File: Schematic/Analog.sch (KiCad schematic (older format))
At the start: 25 parts, among them J1 GS3, SW1 SW_Push_Dual, SW2 SW_Push_Dual, U1 QX14T50B3.6864

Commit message: Brought the schematic and PCB board design up to date.
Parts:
- removed C2: 10uF, Capacitors_THT:CP_Radial_D5.0mm_P2.50mm, symbol CP
- added C20, C21, C22: 0.1uF, Capacitors_THT:C_Disc_D4.7mm_W2.5mm_P5.00mm, symbol C_Small
- added D1: 1N4148, Diodes_THT:D_DO-35_SOD27_P2.54mm_Vertical_AnodeUp, symbol D
- added IC18: NE555, Housings_DIP:DIP-8_W7.62mm_Socket, symbol NE555
- added J2: DataBus Pin Header, Socket_Strips:Socket_Strip_Straight_1x10_Pitch2.54mm, symbol Conn_01x10_Male
- added J3: AddressBus Pin Header, Socket_Strips:Socket_Strip_Straight_1x18_Pitch2.54mm, symbol Conn_01x18_Male
- added R4: 1M, Resistors_THT:R_Axial_DIN0204_L3.6mm_D1.6mm_P1.90mm_Vertical, symbol R
- added R5, R6: 10K, Resistors_THT:R_Axial_DIN0204_L3.6mm_D1.6mm_P1.90mm_Vertical, symbol R
- C1: footprint Capacitors_THT:CP_Radial_D5.0mm_P2.50mm -> Capacitors_THT:CP_Radial_D5.0mm_P2.00mm
- C10, C11, C12, C13, C14, C15, C16, C17, C18, C19, C4, C5, C6, C7, C8, C9: footprint Capacitors_THT:C_Disc_D3.0mm_W1.6mm_P2.50mm -> Capacitors_THT:C_Disc_D4.7mm_W2.5mm_P5.00mm
- C3: footprint Capacitors_THT:CP_Radial_D10.0mm_P2.50mm -> Capacitors_THT:CP_Radial_D8.0mm_P5.00mm
- J1: footprint Connectors:GS3 -> Pin_Headers:Pin_Header_Straight_1x03_Pitch2.54mm
- R1: value 10K -> 20K
- R2: value 10K -> 1K
- U1: value QX14T50B3.6864 -> ECS-100A-035
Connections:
- net GNDREF: now also SW1.3, SW2.3, C20.2, C21.2, IC18.1 (GND), J2.1 (Pin_1), J3.1 (Pin_1); no longer SW1.4, SW2.4
- net VCC: now also C20.1, D1.1 (K), IC18.4 (R), IC18.8 (VCC), R4.1, R5.1, R6.1; no longer R2.1
- net Reset renamed ~Reset
- net ~Reset: now also R2.1; no longer SW1.3
- new net: R2.2, SW1.4
- new net: IC18.3 (Q), J1.3 (G3)
- new net: C22.2, R6.2, SW2.4
- new net: C22.1, D1.2 (A), IC18.2 (TR), R5.2
- new net: C21.1, IC18.6 (THR), IC18.7 (DIS), R4.2
- new net adr0: J3.3 (Pin_3)
- new net adr1: J3.4 (Pin_4)
- new net adr10: J3.13 (Pin_13)
- new net adr11: J3.14 (Pin_14)
- new net adr12: J3.15 (Pin_15)
- new net adr13: J3.16 (Pin_16)
- new net adr14: J3.17 (Pin_17)
- new net adr15: J3.18 (Pin_18)
- new net adr2: J3.5 (Pin_5)
- new net adr3: J3.6 (Pin_6)
- new net adr4: J3.7 (Pin_7)
- new net adr5: J3.8 (Pin_8)
- new net adr6: J3.9 (Pin_9)
- new net adr7: J3.10 (Pin_10)
- new net adr8: J3.11 (Pin_11)
- new net adr9: J3.12 (Pin_12)
- new net d0: J2.3 (Pin_3)
- new net d1: J2.4 (Pin_4)
- new net d2: J2.5 (Pin_5)
- new net d3: J2.6 (Pin_6)
- new net d4: J2.7 (Pin_7)
- new net d5: J2.8 (Pin_8)
- new net d6: J2.9 (Pin_9)
- new net d7: J2.10 (Pin_10)
- no-connect marks 5 -> 8
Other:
- note added: "3.5MHz oscillator"
- note added: "555 circuit from https://electronics.stackexchange.com/questions/180716/555-timer-one-shot-trigger"
- note added: "AddressBus"
- note added: "Clock generation"
- note added: "DataBus"
- note added: "Logic levels"
- note added: "Reset generation"
- note removed: "3.68MHz oscillator"
- moved on the sheet: C1, C10, C11, C12, C13, C14, C15, C16, C17, C18, C19, C3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

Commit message: Brought the schematic up to date with the wiring from the TTL verilog version.
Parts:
- added IC15: 74HCT139, symbol 74LS139
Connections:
- net Clk: now also IC15.14 (A0)
- net GNDREF: now also IC15.13 (A1), IC15.15 (E)
- net VCC: now also IC15.16 (VCC)
- new net GND: IC15.8 (GND)
- no-connect marks 8 -> 11
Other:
- note added: "Clkbar is an inverted Clk signal, used to initiate events on the\nfalling edge of Clk. We use the spare 139 half as an inverter."
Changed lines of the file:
@@
 Text Notes 750  7650 0    60   ~ 0
 555 circuit from https://electronics.stackexchange.com/questions/180716/555-timer-one-shot-trigger
+$Comp
+L 74LS139 IC15
+U 2 1 5CC0FB47
+P 7750 4700
+F 0 "IC15" H 7750 5250 50  0000 C CNN
+F 1 "74HCT139" H 7750 5150 50  0000 C CNN
+F 2 "" H 7750 4700 50  0001 C CNN
+F 3 "" H 7750 4700 50  0001 C CNN
+	2    7750 4700
+	1    0    0    -1
+$EndComp
+Text GLabel 6650 4600 0    60   Input ~ 0
+Clk
+Wire Wire Line
+	6900 4600 6650 4600
+Text GLabel 6600 4450 0    60   Input ~ 0
+Lo
+Text GLabel 6600 4950 0    60   Input ~ 0
+Lo
+Wire Wire Line
+	6600 4450 6900 4450
+Wire Wire Line
+	6600 4950 6900 4950
+Text GLabel 9250 4600 0    60   Output ~ 0
+~Clkbar
+Wire Wire Line
+	8600 4600 8900 4600
+NoConn ~ 8600 4400
+NoConn ~ 8600 4800
+NoConn ~ 8600 5000
+Text Notes 6400 5400 0    60   ~ 0
+Clkbar is an inverted Clk signal, used to initiate events on the\nfalling edge of Clk. We use the spare 139 half as an inverter.
 $EndSCHEMATC

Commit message: Updated the schematic and also moved to KiCad 5.
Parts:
- removed J1: GS3, Pin_Headers:Pin_Header_Straight_1x03_Pitch2.54mm, symbol GS3
- removed J2: DataBus Pin Header, Socket_Strips:Socket_Strip_Straight_1x10_Pitch2.54mm, symbol Conn_01x10_Male
- removed J3: AddressBus Pin Header, Socket_Strips:Socket_Strip_Straight_1x18_Pitch2.54mm, symbol Conn_01x18_Male
- added J1: Jumper_3_Bridged12, Connector_PinSocket_2.54mm:PinSocket_1x03_P2.54mm_Vertical, symbol Jumper:Jumper_3_Bridged12
- added J2: Data Bus Pin Header, Connector_PinSocket_2.54mm:PinSocket_1x10_P2.54mm_Vertical, symbol Connector:Conn_01x10_Female
- added J3: Address Bus Pin Header, Connector_PinSocket_2.54mm:PinSocket_1x18_P2.54mm_Vertical, symbol Connector:Conn_01x18_Female
- C1, C3: symbol CP -> Device:CP
- C10, C11, C12, C13, C14, C15, C16, C17, C18, C19, C4, C5, C6, C7, C8, C9: symbol C -> Device:C
- C20, C21, C22: symbol C_Small -> Device:C_Small
- D1: symbol D -> Device:D
- IC15: footprint (none) -> Package_DIP:DIP-16_W7.62mm_Socket; symbol 74LS139 -> 74xx:74LS139
- IC18: symbol NE555 -> Timer:NE555
- R1, R2, R4, R5, R6: symbol R -> Device:R
- SW1, SW2: symbol SW_Push_Dual -> Switch:SW_Push_Dual
- U1: symbol QX14T50B1.843200B50TT -> QX14T50B1.843200B50TT:QX14T50B1.843200B50TT
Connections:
- net Clk: now also J1.2 (C)
- net GNDREF: now also J2.10 (Pin_10), J3.18 (Pin_18)
- net VCC: no longer IC15.16 (VCC)
- net adr0: now also J3.16 (Pin_16)
- net adr1: now also J3.15 (Pin_15)
- net adr10: now also J3.6 (Pin_6)
- net adr11: now also J3.5 (Pin_5)
- net adr12: now also J3.4 (Pin_4)
- net adr13: now also J3.3 (Pin_3)
- net adr14: now also J3.2 (Pin_2)
- net adr15: now also J3.1 (Pin_1)
- net adr2: now also J3.14 (Pin_14)
- net adr3: now also J3.13 (Pin_13)
- net adr4: now also J3.12 (Pin_12)
- net adr5: now also J3.11 (Pin_11)
- net adr6: now also J3.10 (Pin_10)
- net adr7: now also J3.9 (Pin_9)
- net adr8: now also J3.8 (Pin_8)
- net adr9: now also J3.7 (Pin_7)
- net d0: now also J2.8 (Pin_8)
- net d1: now also J2.7 (Pin_7)
- net d2: now also J2.6 (Pin_6)
- net d3: now also J2.5 (Pin_5)
- net d4: now also J2.4 (Pin_4)
- net d5: now also J2.3 (Pin_3)
- net d6: now also J2.2 (Pin_2)
- net d7: now also J2.1 (Pin_1)
- net ~Clkbar: now also IC15.11 (O1)
- net at U1.8 (OUTPUT): now also J1.3 (B)
- net at IC18.3 (Q): now also J1.1 (A)
- removed net GND: IC15.8 (GND)
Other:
- note added: "555 circuit from\nhttps://electronics.stackexchange.com/questions/180716/555-timer-one-shot-trigger"
- note removed: "555 circuit from https://electronics.stackexchange.com/questions/180716/555-timer-one-shot-trigger"

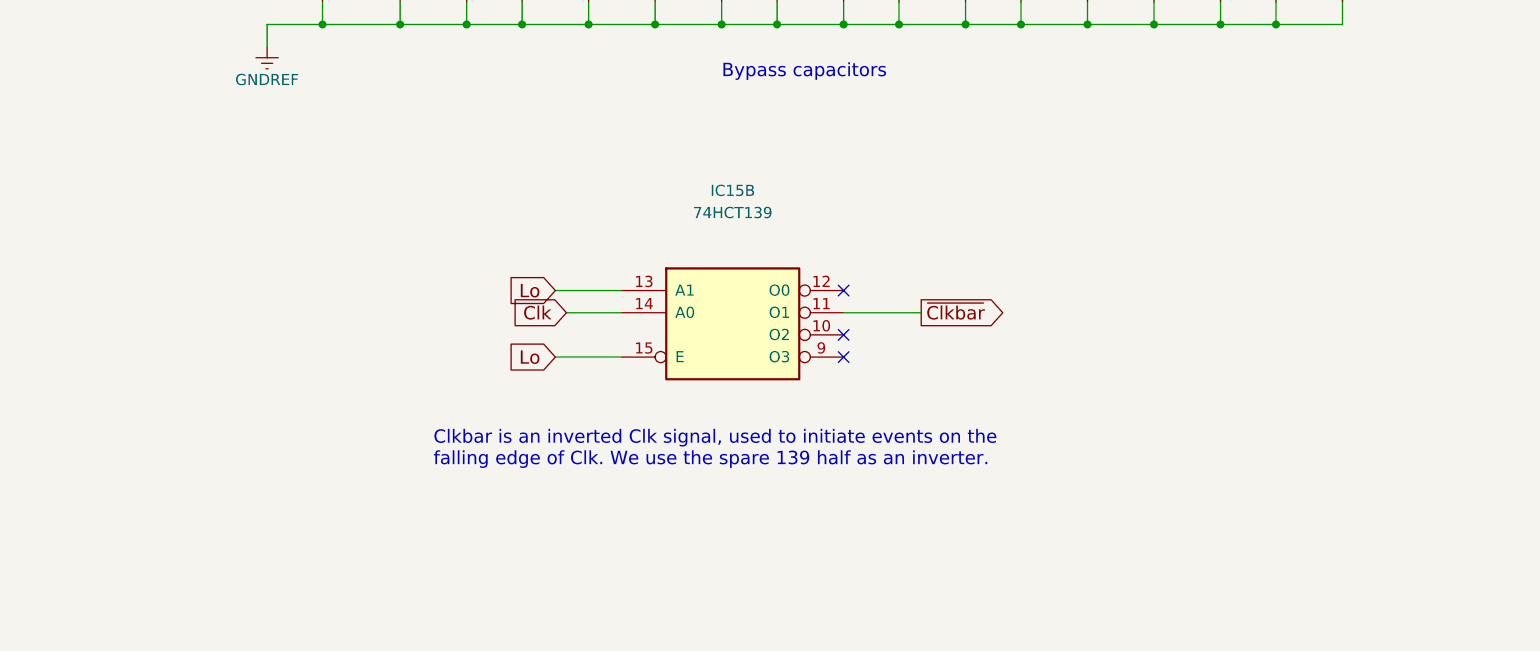
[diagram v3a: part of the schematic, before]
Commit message: Updated the PCB and schematic to have a 330pF capacitor to fix the "jump" glitch that I've been experiencing.
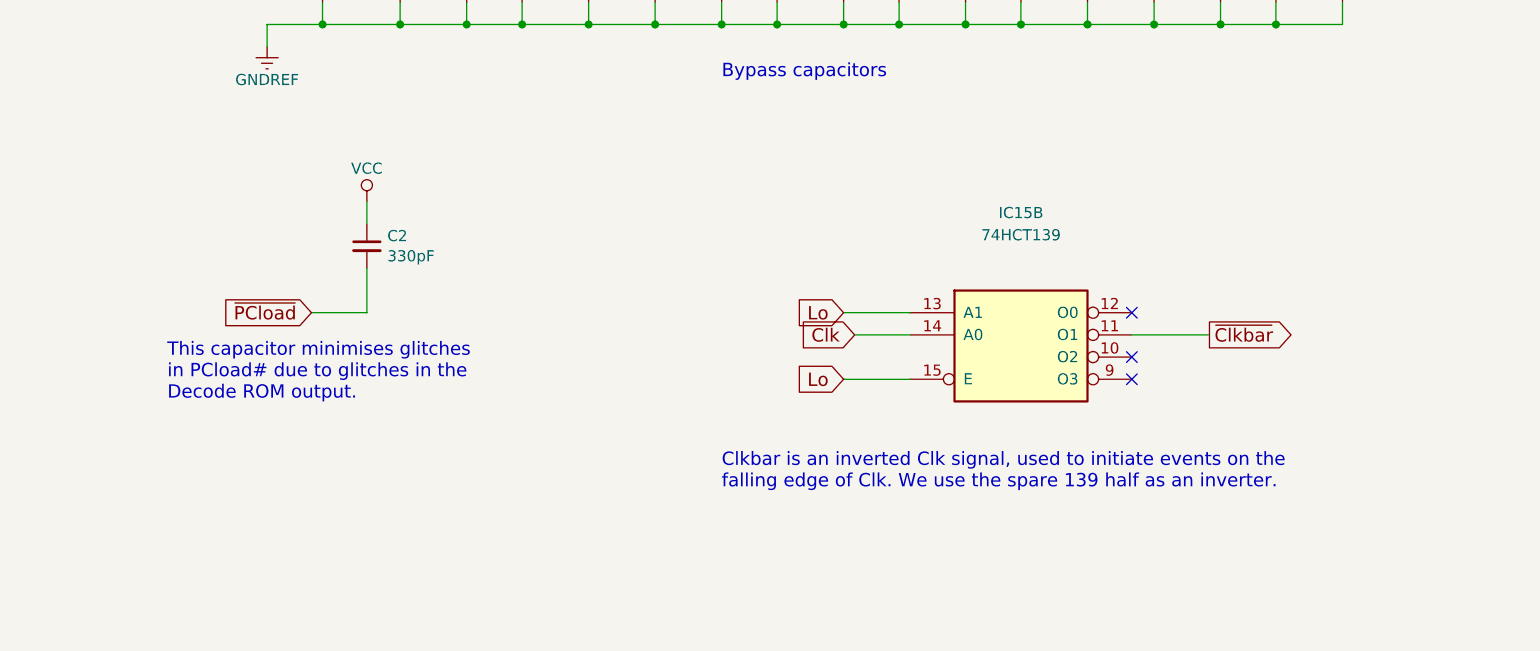
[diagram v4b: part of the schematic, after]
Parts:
- added C2: 330pF, Capacitor_THT:C_Disc_D4.7mm_W2.5mm_P5.00mm, symbol Device:C_Small
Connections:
- net VCC: now also C2.1
- new net ~PCload: C2.2
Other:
- note added: "This capacitor minimises glitches\nin PCload# due to glitches in the\nDecode ROM output."
- moved on the sheet: IC15B
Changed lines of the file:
@@
 L 74xx:74LS139 IC15
 U 2 1 5CC0FB47
-P 7750 4700
-F 0 "IC15" H 7750 5250 50  0000 C CNN
-F 1 "74HCT139" H 7750 5150 50  0000 C CNN
-F 2 "Package_DIP:DIP-16_W7.62mm_Socket" H 7750 4700 50  0001 C CNN
-F 3 "" H 7750 4700 50  0001 C CNN
-	2    7750 4700
+P 9050 4800
+F 0 "IC15" H 9050 5350 50  0000 C CNN
+F 1 "74HCT139" H 9050 5250 50  0000 C CNN
+F 2 "Package_DIP:DIP-16_W7.62mm_Socket" H 9050 4800 50  0001 C CNN
+F 3 "" H 9050 4800 50  0001 C CNN
+	2    9050 4800
 	1    0    0    -1
 $EndComp
-Text GLabel 7000 4700 0    60   Input ~ 0
+Text GLabel 8300 4800 0    60   Input ~ 0
 Clk
 Wire Wire Line
-	7250 4700 7000 4700
-Text GLabel 6950 4600 0    60   Input ~ 0
+	8550 4800 8300 4800
+Text GLabel 8250 4700 0    60   Input ~ 0
 Lo
-Text GLabel 6950 4900 0    60   Input ~ 0
+Text GLabel 8250 5000 0    60   Input ~ 0
 Lo
 Wire Wire Line
-	6950 4600 7250 4600
+	8250 4700 8550 4700
 Wire Wire Line
-	6950 4900 7250 4900
-Text GLabel 8600 4700 2    60   Output ~ 0
+	8250 5000 8550 5000
+Text GLabel 9900 4800 2    60   Output ~ 0
 ~Clkbar
-NoConn ~ 8250 4600
-NoConn ~ 8250 4800
-NoConn ~ 8250 4900
-Text Notes 6400 5400 0    60   ~ 0
+NoConn ~ 9550 4700
+NoConn ~ 9550 4900
+NoConn ~ 9550 5000
+Text Notes 7700 5500 0    60   ~ 0
 Clkbar is an inverted Clk signal, used to initiate events on the\nfalling edge of Clk. We use the spare 139 half as an inverter.
 Wire Wire Line
@@
 $EndComp
 Wire Wire Line
-	8250 4700 8600 4700
+	9550 4800 9900 4800
+Text GLabel 5850 4700 0    60   Input ~ 0
+~PCload
+$Comp
+L power:VCC #PWR0104
+U 1 1 5CF39113
+P 6100 4200
+F 0 "#PWR0104" H 6100 4050 50  0001 C CNN
+F 1 "VCC" H 6100 4350 50  0000 C CNN
+F 2 "" H 6100 4200 50  0001 C CNN
+F 3 "" H 6100 4200 50  0001 C CNN
+	1    6100 4200
+	1    0    0    -1
+$EndComp
+Wire Wire Line
+	6100 4200 6100 4300
+Text Notes 5200 5100 0    60   ~ 0
+This capacitor minimises glitches\nin PCload# due to glitches in the\nDecode ROM output.
+$Comp
+L Device:C_Small C2
+U 1 1 5CF599C2
+P 6100 4400
+F 0 "C2" H 6192 4446 50  0000 L CNN
+F 1 "330pF" H 6192 4355 50  0000 L CNN
+F 2 "Capacitor_THT:C_Disc_D4.7mm_W2.5mm_P5.00mm" H 6100 4400 50  0001 C CNN
+F 3 "~" H 6100 4400 50  0001 C CNN
+	1    6100 4400
+	1    0    0    -1
+$EndComp
+Wire Wire Line
+	5850 4700 6100 4700
+Wire Wire Line
+	6100 4700 6100 4500
 Wire Bus Line
 	2500 4800 2500 5850

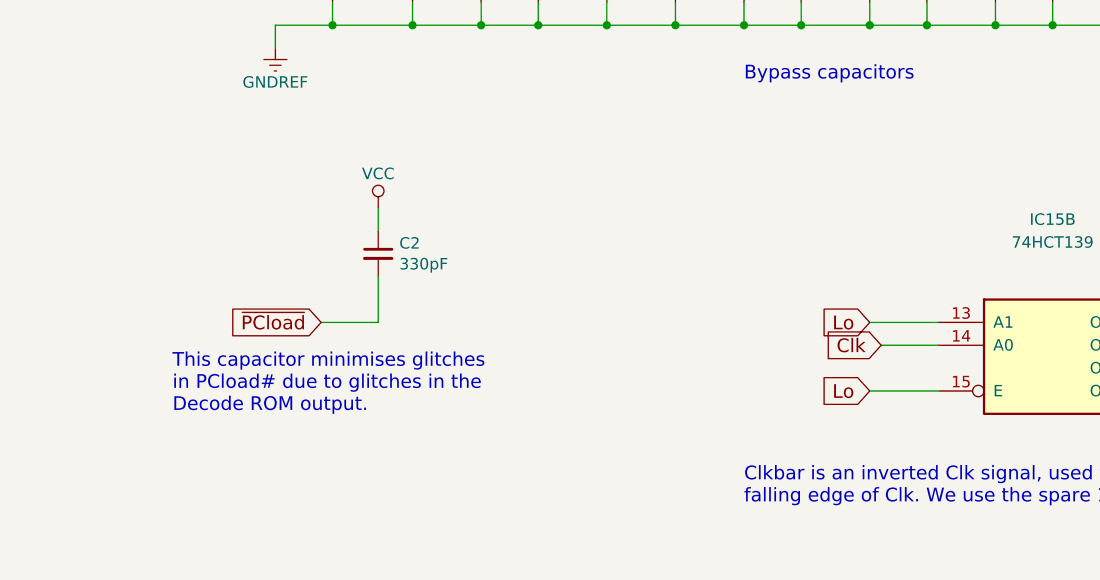
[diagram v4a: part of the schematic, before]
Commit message: I've updated the schematic and the PCB to have the 74HCT151 chip.
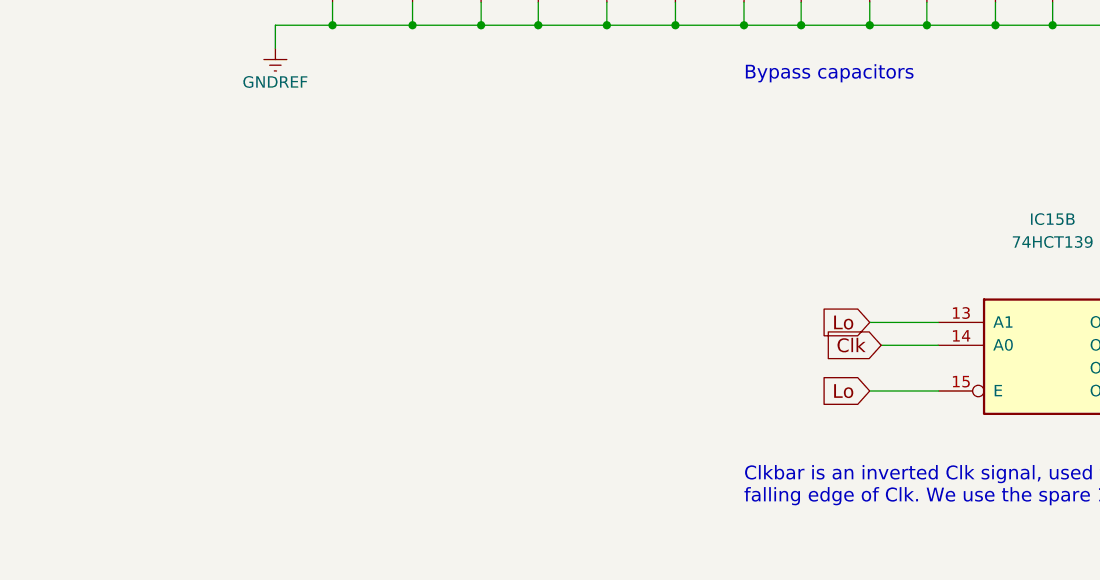
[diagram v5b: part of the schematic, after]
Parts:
- removed C2: 330pF, Capacitor_THT:C_Disc_D4.7mm_W2.5mm_P5.00mm, symbol Device:C_Small
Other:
- note removed: "This capacitor minimises glitches\nin PCload# due to glitches in the\nDecode ROM output."
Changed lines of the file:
@@
 Text GLabel 8300 4800 0    60   Input ~ 0
 Clk
-Wire Wire Line
-	8550 4800 8300 4800
 Text GLabel 8250 4700 0    60   Input ~ 0
 Lo
@@
 Wire Wire Line
 	9550 4800 9900 4800
-Text GLabel 5850 4700 0    60   Input ~ 0
-~PCload
-$Comp
-L power:VCC #PWR0104
-U 1 1 5CF39113
-P 6100 4200
-F 0 "#PWR0104" H 6100 4050 50  0001 C CNN
-F 1 "VCC" H 6100 4350 50  0000 C CNN
-F 2 "" H 6100 4200 50  0001 C CNN
-F 3 "" H 6100 4200 50  0001 C CNN
-	1    6100 4200
-	1    0    0    -1
-$EndComp
 Wire Wire Line
-	6100 4200 6100 4300
-Text Notes 5200 5100 0    60   ~ 0
-This capacitor minimises glitches\nin PCload# due to glitches in the\nDecode ROM output.
-$Comp
-L Device:C_Small C2
-U 1 1 5CF599C2
-P 6100 4400
-F 0 "C2" H 6192 4446 50  0000 L CNN
-F 1 "330pF" H 6192 4355 50  0000 L CNN
-F 2 "Capacitor_THT:C_Disc_D4.7mm_W2.5mm_P5.00mm" H 6100 4400 50  0001 C CNN
-F 3 "~" H 6100 4400 50  0001 C CNN
-	1    6100 4400
-	1    0    0    -1
-$EndComp
-Wire Wire Line
-	5850 4700 6100 4700
-Wire Wire Line
-	6100 4700 6100 4500
+	8300 4800 8550 4800
 Wire Bus Line
 	2500 4800 2500 5850
